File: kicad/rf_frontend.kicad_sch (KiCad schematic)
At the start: 52 parts, among them U10 AD8350ARZ20-REEL7, U20 PE43711B-Z, U21 LTC2386CUH-16-PBF

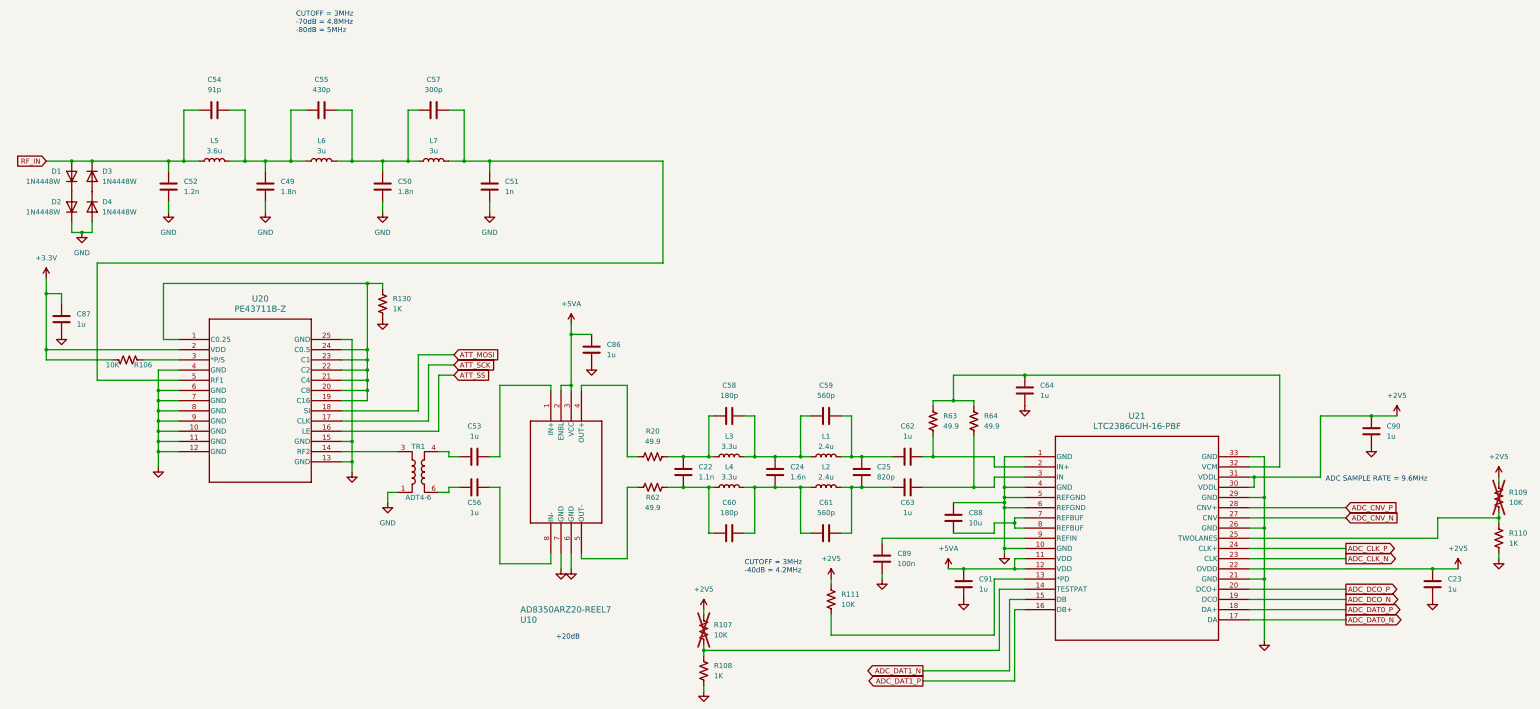
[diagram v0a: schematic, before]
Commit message: add net names
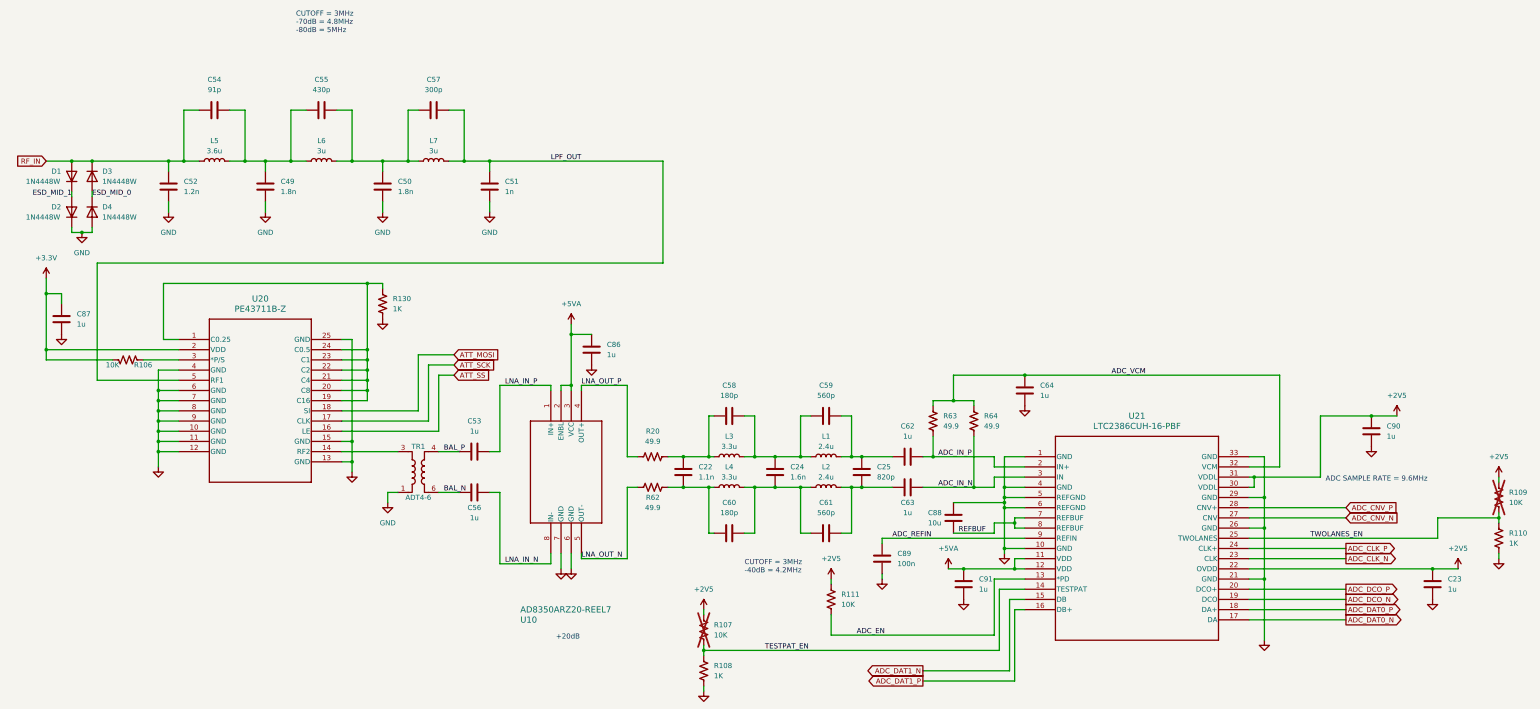
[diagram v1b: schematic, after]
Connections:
- net LPF_OUT: now reaches C51.1, C57.2, L7.2, U20.5 (RF1)
- net ESD_MID_1: now reaches D1.1 (K), D2.2 (A)
- net ADC_EN: now reaches R111.2, U21.13 (*PD)
- net TESTPAT_EN: now reaches R107.2, R108.1, U21.14 (TESTPAT)
- net ADC_IN_P: now reaches C62.2, R63.2, U21.2 (IN+)
- net TWOLANES_EN: now reaches R109.2, R110.1, U21.25 (TWOLANES)
- net ADC_IN_N: now reaches C63.2, R64.2, U21.3 (IN)
- net ADC_VCM: now reaches C64.1, R63.1, R64.1, U21.32 (VCM)
- net REFBUF: now reaches C88.2, U21.7 (REFBUF), U21.8 (REFBUF)
- net ADC_REFIN: now reaches C89.1, U21.9 (REFIN)
- net BAL_N: now reaches C56.1, TR1.6
- net LNA_IN_N: now reaches C56.2, U10.8 (IN-)
- net ESD_MID_0: now reaches D3.2 (A), D4.1 (K)
- net LNA_OUT_P: now reaches R20.1, U10.4 (OUT+)
- net BAL_P: now reaches C53.1, TR1.4
- net LNA_IN_P: now reaches C53.2, U10.1 (IN+)
- net LNA_OUT_N: now reaches R62.1, U10.5 (OUT-)
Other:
- moved on the sheet: C53, C56, D2, D4

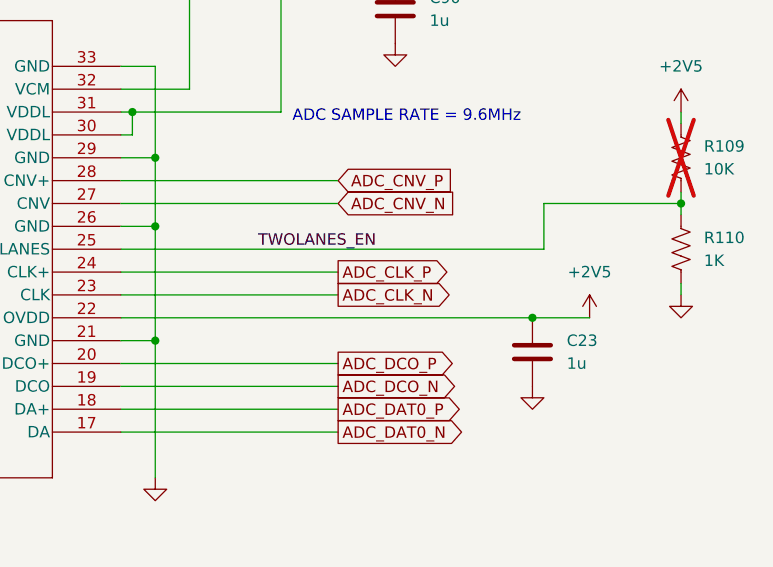
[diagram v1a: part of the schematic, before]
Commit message: fix adc_clk, adp7118
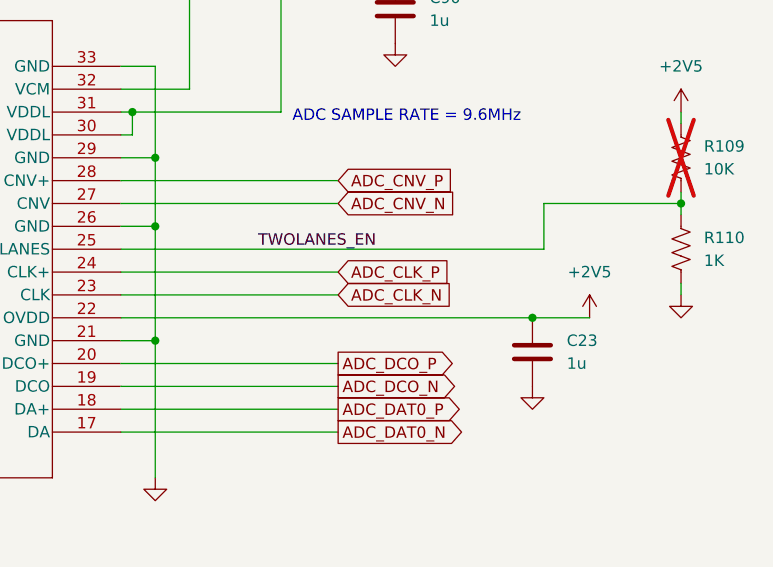
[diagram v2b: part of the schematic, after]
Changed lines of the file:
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@@
     )
   )
-  (global_label "ADC_CLK_P" (shape output) (at 354.33 179.07 0) (fields_autoplaced)
+  (global_label "ADC_CLK_P" (shape input) (at 354.33 179.07 0) (fields_autoplaced)
     (effects (font (size 1.27 1.27)) (justify left))
     (property "Intersheetrefs" "${INTERSHEET_REFS}" (at 367.7171 179.07 0)
@@
     )
   )
-  (global_label "ADC_CLK_N" (shape output) (at 354.33 181.61 0) (fields_autoplaced)
+  (global_label "ADC_CLK_N" (shape input) (at 354.33 181.61 0) (fields_autoplaced)
     (effects (font (size 1.27 1.27)) (justify left))
     (property "Intersheetrefs" "${INTERSHEET_REFS}" (at 367.7776 181.61 0)

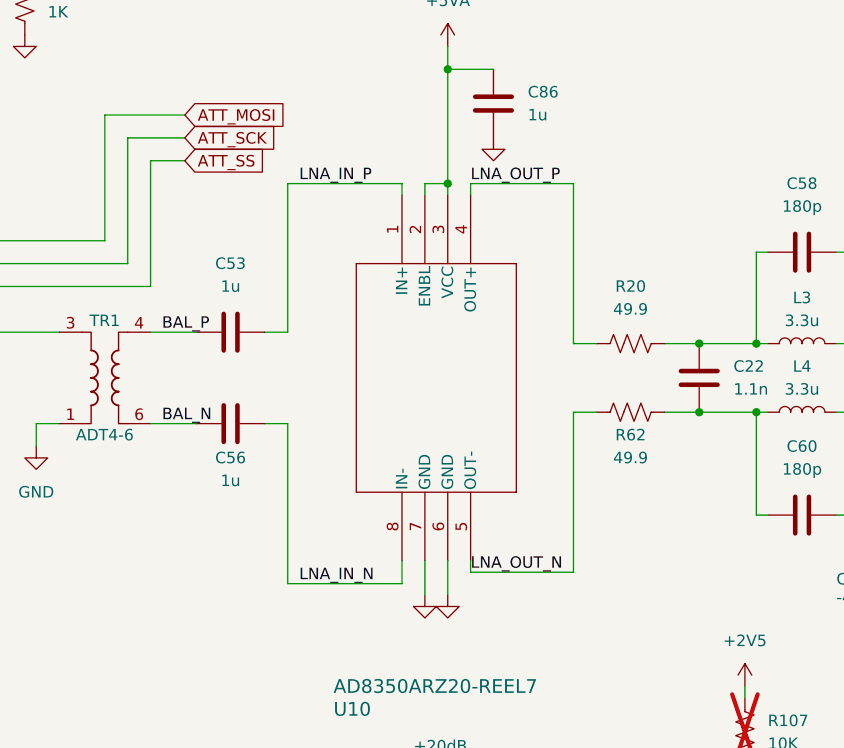
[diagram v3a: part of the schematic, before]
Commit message: fix schematic to align w/ pcb
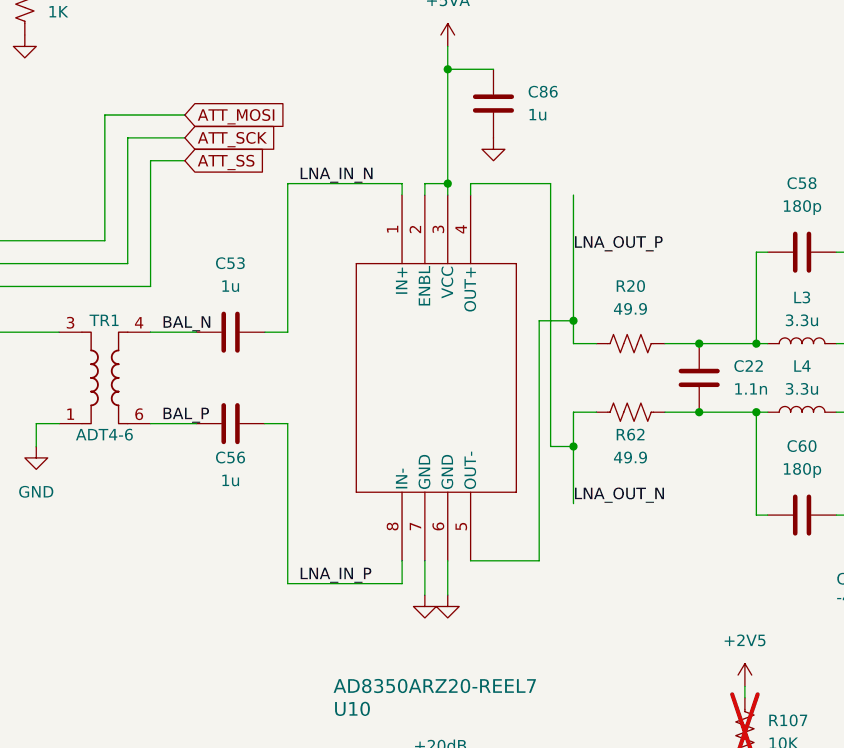
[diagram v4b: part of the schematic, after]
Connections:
- net BAL_N: now also C53.1, TR1.4; no longer C56.1, TR1.6
- net BAL_P: now also C56.1, TR1.6; no longer C53.1, TR1.4
- net LNA_IN_N: now also C53.2, U10.1 (IN+); no longer C56.2, U10.8 (IN-)
- net LNA_IN_P: now also C56.2, U10.8 (IN-); no longer C53.2, U10.1 (IN+)
- net LNA_OUT_N: now also U10.4 (OUT+); no longer U10.5 (OUT-)
- net LNA_OUT_P: now also U10.5 (OUT-); no longer U10.4 (OUT+)
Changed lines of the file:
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@@
+	)
+	(junction
+		(at 175.26 167.64)
+		(diameter 0)
+		(color 0 0 0 0)
 	)
 	(junction
@@
 	)
 	(junction
+		(at 175.26 153.67)
+		(diameter 0)
+		(color 0 0 0 0)
+	)
+	(junction
 		(at 218.44 163.83)
 		(diameter 0)
@@
 	(wire
 		(pts
+			(xy 175.26 167.64) (xy 175.26 173.99)
+		)
+		(stroke
+			(width 0)
+			(type default)
+		)
+	)
+	(wire
+		(pts
 			(xy 271.78 181.61) (xy 271.78 184.15)
 		)
@@
 	(wire
 		(pts
-			(xy 175.26 181.61) (xy 175.26 163.83)
+			(xy 175.26 163.83) (xy 175.26 167.64)
 		)
 		(stroke
@@
 	(wire
 		(pts
+			(xy 163.83 139.7) (xy 163.83 138.43)
+		)
+		(stroke
+			(width 0)
+			(type default)
+		)
+	)
+	(wire
+		(pts
 			(xy 331.47 161.29) (xy 347.98 161.29)
 		)
@@
 	(wire
 		(pts
-			(xy 175.26 138.43) (xy 175.26 156.21)
+			(xy 171.45 180.34) (xy 171.45 153.67)
 		)
 		(stroke
@@
 	(wire
 		(pts
-			(xy 163.83 180.34) (xy 163.83 181.61)
-		)
-		(stroke
-			(width 0)
-			(type default)
-		)
-	)
-	(wire
-		(pts
 			(xy 189.23 163.83) (xy 195.58 163.83)
 		)
@@
 	(wire
 		(pts
+			(xy 171.45 153.67) (xy 175.26 153.67)
+		)
+		(stroke
+			(width 0)
+			(type default)
+		)
+	)
+	(wire
+		(pts
 			(xy 134.62 82.55) (xy 140.97 82.55)
 		)
@@
 	(wire
 		(pts
+			(xy 172.72 167.64) (xy 175.26 167.64)
+		)
+		(stroke
+			(width 0)
+			(type default)
+		)
+	)
+	(wire
+		(pts
 			(xy 251.46 151.13) (xy 251.46 156.21)
 		)
@@
 	(wire
 		(pts
+			(xy 175.26 139.7) (xy 175.26 153.67)
+		)
+		(stroke
+			(width 0)
+			(type default)
+		)
+	)
+	(wire
+		(pts
 			(xy 228.6 156.21) (xy 231.14 156.21)
 		)
@@
 	(wire
 		(pts
-			(xy 163.83 181.61) (xy 175.26 181.61)
+			(xy 172.72 138.43) (xy 172.72 167.64)
 		)
 		(stroke
@@
 	(wire
 		(pts
-			(xy 163.83 138.43) (xy 175.26 138.43)
-		)
-		(stroke
-			(width 0)
-			(type default)
-		)
-	)
-	(wire
-		(pts
 			(xy 330.2 184.15) (xy 375.92 184.15)
 		)
@@
 	(wire
 		(pts
+			(xy 163.83 180.34) (xy 171.45 180.34)
+		)
+		(stroke
+			(width 0)
+			(type default)
+		)
+	)
+	(wire
+		(pts
 			(xy 156.21 182.88) (xy 156.21 180.34)
 		)
@@
 	(wire
 		(pts
+			(xy 163.83 138.43) (xy 172.72 138.43)
+		)
+		(stroke
+			(width 0)
+			(type default)
+		)
+	)
+	(wire
+		(pts
 			(xy 231.14 163.83) (xy 233.68 163.83)
 		)
@@
 	(wire
 		(pts
-			(xy 163.83 139.7) (xy 163.83 138.43)
-		)
-		(stroke
-			(width 0)
-			(type default)
-		)
-	)
-	(wire
-		(pts
 			(xy 30.48 82.55) (xy 36.83 82.55)
 		)
@@
 		(pts
 			(xy 68.58 69.85) (xy 64.77 69.85)
+		)
+		(stroke
+			(width 0)
+			(type default)
+		)
+	)
+	(wire
+		(pts
+			(xy 175.26 153.67) (xy 175.26 156.21)
 		)
 		(stroke
@@
 	)
 	(label "LNA_OUT_N"
-		(at 163.83 181.61 0)
+		(at 175.26 173.99 0)
 		(fields_autoplaced yes)
 		(effects
@@
 		)
 	)
-	(label "LNA_IN_N"
+	(label "LNA_IN_P"
 		(at 144.78 182.88 0)
 		(fields_autoplaced yes)
@@
 		)
 	)
-	(label "BAL_P"
+	(label "BAL_N"
 		(at 129.54 154.94 0)
 		(fields_autoplaced yes)
@@
 		)
 	)
-	(label "LNA_IN_P"
+	(label "LNA_IN_N"
 		(at 144.78 138.43 0)
 		(fields_autoplaced yes)
@@
 		)
 	)
-	(label "BAL_N"
+	(label "BAL_P"
 		(at 129.54 165.1 0)
 		(fields_autoplaced yes)
@@
 	)
 	(label "LNA_OUT_P"
-		(at 163.83 138.43 0)
+		(at 175.26 146.05 0)
 		(fields_autoplaced yes)
 		(effects
